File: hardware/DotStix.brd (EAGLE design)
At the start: 20.3 x 50 mm, 29 parts, among them IC2 SI1145, U1 ATMEGA328P-MU-QFN32, U2 TMP102, U4 9DoF IMU

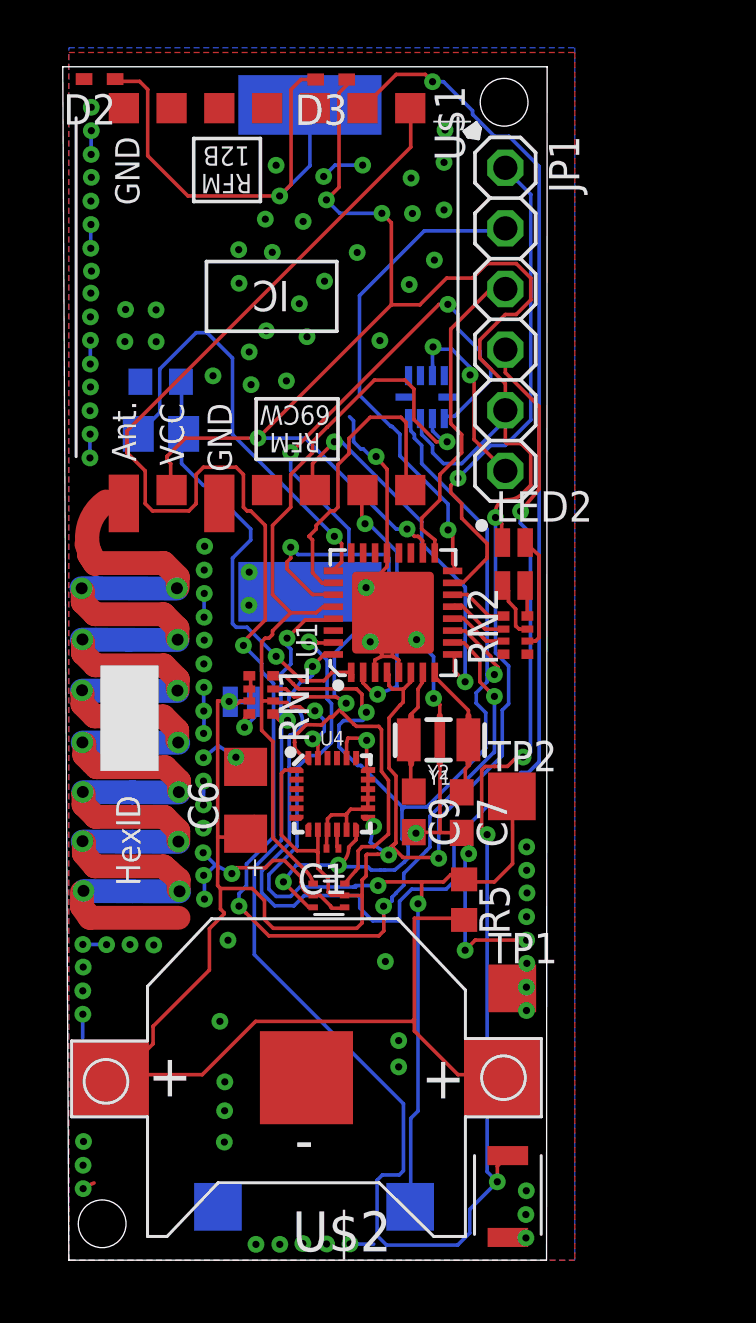
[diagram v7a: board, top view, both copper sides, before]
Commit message: Move solar panel further away from UV sensor
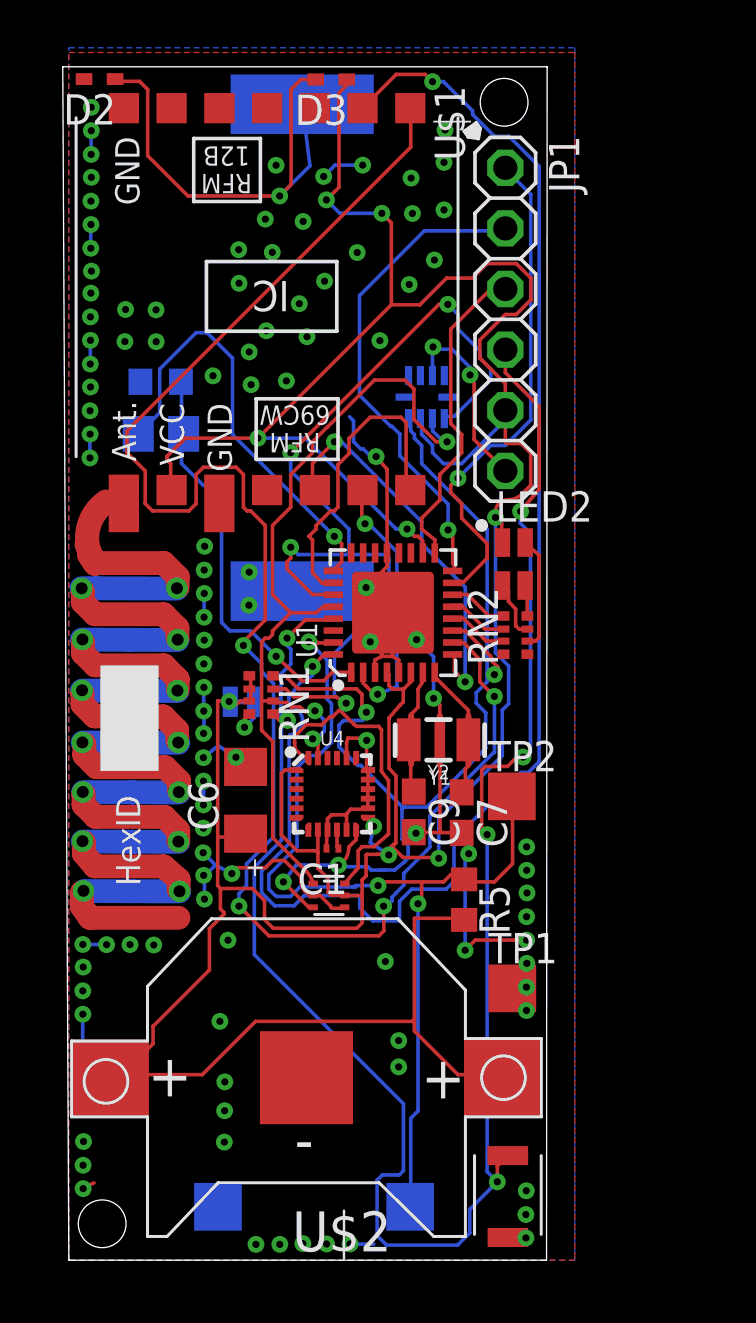
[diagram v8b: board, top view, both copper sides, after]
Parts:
- moved D1 0.32 mm to (9.78, 38.2)
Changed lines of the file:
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@@
 <layer number="46" name="Milling" color="3" fill="1" visible="no" active="yes"/>
 <layer number="47" name="Measures" color="7" fill="1" visible="no" active="yes"/>
-<layer number="48" name="Document" color="7" fill="1" visible="no" active="yes"/>
+<layer number="48" name="Document" color="7" fill="1" visible="yes" active="yes"/>
 <layer number="49" name="Reference" color="7" fill="1" visible="no" active="yes"/>
 <layer number="50" name="dxf" color="7" fill="1" visible="no" active="no"/>
@@
 <attribute name="TP_SIGNAL_NAME" value="" x="18.56231875" y="19.433540625" size="1.778" layer="27" display="off"/>
 </element>
-<element name="D1" library="SparkFun" package="SOLARBIT-12X1" value="SOLAR-IXYS-" x="10.101578125" y="38.204140625" rot="MR270"/>
+<element name="D1" library="SparkFun" package="SOLARBIT-12X1" value="SOLAR-IXYS-" x="9.778996875" y="38.23208125" rot="MR270"/>
 <element name="D2" library="diode" package="SOD523" value="" x="1.338575" y="49.486821875" rot="R180"/>
 <element name="D3" library="diode" package="SOD523" value="" x="11.041378125" y="49.47158125" rot="R180"/>
@@
 <via x="12.45361875" y="28.178759375" extent="1-16" drill="0.3"/>
 <wire x1="12.45361875" y1="28.178759375" x2="10.276196875" y2="28.178759375" width="0.1524" layer="16"/>
-<wire x1="10.276196875" y1="28.178759375" x2="10.101578125" y2="28.004140625" width="0.1524" layer="16"/>
+<wire x1="10.276196875" y1="28.178759375" x2="9.778996875" y2="28.03208125" width="0.1524" layer="16"/>
 <wire x1="13.331378125" y1="29.629740625" x2="13.331378125" y2="29.05651875" width="0.1524" layer="1"/>
 <wire x1="13.331378125" y1="29.05651875" x2="12.45361875" y2="28.178759375" width="0.1524" layer="1"/>
@@
 <contactref element="D3" pad="A"/>
 <contactref element="D1" pad="+"/>
-<wire x1="10.101578125" y1="48.404140625" x2="10.101578125" y2="45.857159375" width="0.1524" layer="16"/>
+<wire x1="9.778996875" y1="48.43208125" x2="10.101578125" y2="45.857159375" width="0.1524" layer="16"/>
 <wire x1="10.101578125" y1="45.857159375" x2="8.83411875" y2="44.5897" width="0.1524" layer="16"/>
 <via x="8.83411875" y="44.5897" extent="1-16" drill="0.3"/>
@@
 <wire x1="11.8872" y1="24.384" x2="11.8872" y2="24.5364" width="0.1524" layer="1"/>
 <wire x1="8.6868" y1="25.2984" x2="9.776459375" y2="24.274778125" width="0.1524" layer="1"/>
-<wire x1="7.4676" y1="26.5176" x2="8.6868" y2="25.2984" width="0.1524" layer="16"/>
-<wire x1="7.0104" y1="26.5176" x2="7.4676" y2="26.5176" width="0.1524" layer="16"/>
-<wire x1="6.858" y1="29.4132" x2="6.858" y2="26.67" width="0.1524" layer="16"/>
-<wire x1="7.62" y1="30.1752" x2="6.858" y2="29.4132" width="0.1524" layer="16"/>
-<wire x1="7.62" y1="30.6324" x2="7.62" y2="30.1752" width="0.1524" layer="16"/>
-<wire x1="5.7912" y1="32.4612" x2="7.62" y2="30.6324" width="0.1524" layer="16"/>
 <wire x1="5.6388" y1="32.4612" x2="5.7912" y2="32.4612" width="0.1524" layer="16"/>
 <wire x1="4.7244" y1="33.3756" x2="5.6388" y2="32.4612" width="0.1524" layer="16"/>
@@
 <wire x1="4.7244" y1="34.7472" x2="4.8108" y2="34.6202" width="0.1524" layer="16"/>
 <via x="8.6868" y="25.2984" extent="1-16" drill="0.3"/>
-<wire x1="6.858" y1="26.67" x2="7.0104" y2="26.5176" width="0.1524" layer="16"/>
 <wire x1="11.03058125" y1="24.629740625" x2="11.831378125" y2="24.629740625" width="0.1524" layer="1"/>
 <wire x1="9.776459375" y1="24.274778125" x2="10.68831875" y2="24.27985625" width="0.1524" layer="1"/>
 <wire x1="10.68831875" y1="24.27985625" x2="11.03058125" y2="24.629740625" width="0.1524" layer="1"/>
+<wire x1="5.7912" y1="32.4612" x2="6.4008" y2="31.8516" width="0.1524" layer="16"/>
+<wire x1="6.4008" y1="31.8516" x2="6.4008" y2="26.718259375" width="0.1524" layer="16"/>
+<wire x1="6.4008" y1="26.718259375" x2="6.75131875" y2="26.367740625" width="0.1524" layer="16"/>
+<wire x1="6.75131875" y1="26.367740625" x2="7.617459375" y2="26.367740625" width="0.1524" layer="16"/>
+<wire x1="7.617459375" y1="26.367740625" x2="8.6868" y2="25.2984" width="0.1524" layer="16"/>
 </signal>
 <signal name="LIGHT_SENSE_ENA">
